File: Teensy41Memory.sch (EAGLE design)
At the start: 17 parts, among them IC1 25AA080SN, IC2 25AA080SN, IC3 25AA080SN, IC4 25AA080SN, IC5 25AA080SN, IC6 25AA080SN, IC7 25AA080SN, IC8 25AA080SN, IC9 74AC138D

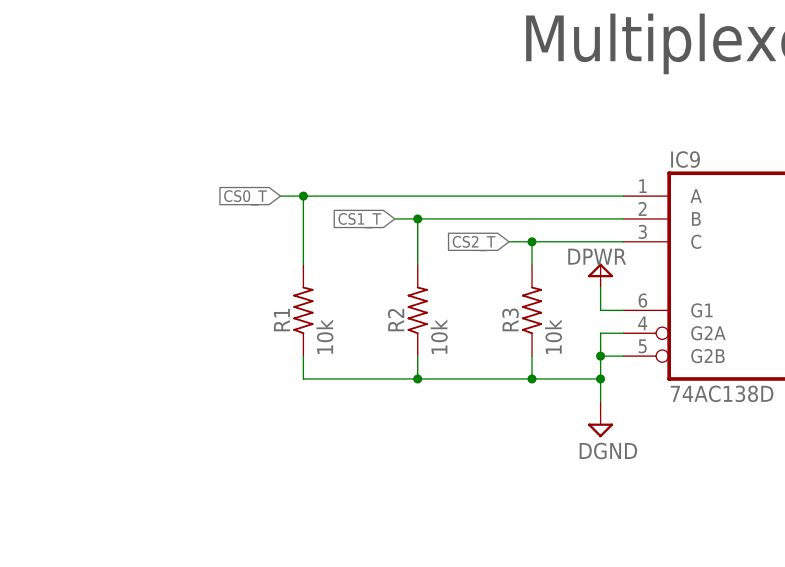
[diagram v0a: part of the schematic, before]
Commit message: Breakout pin 4 of 74AC138 to disable all CS
It is now possible to set all eight chip selects HIGH on the output of 74AC138 by setting pin4 HIGH. The pin is available on Teensy 4.1 pin 5.
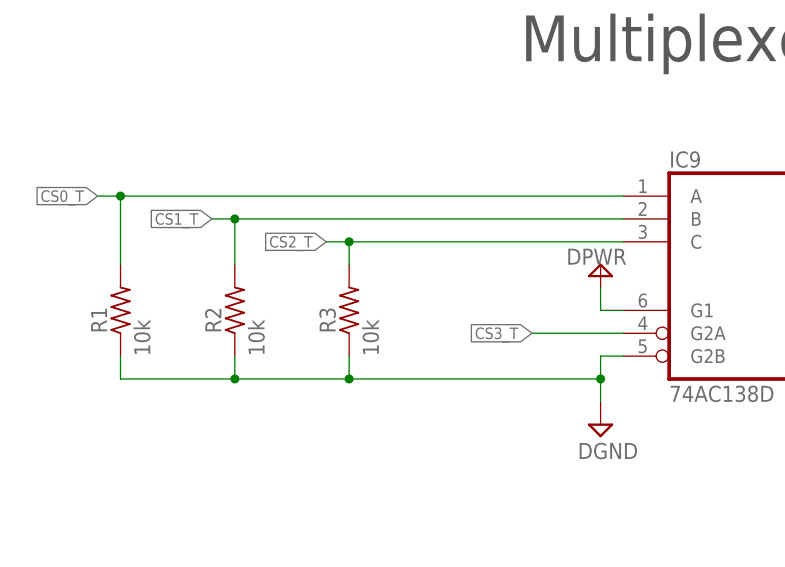
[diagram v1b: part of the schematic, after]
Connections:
- new net CS3_T: IC9A.G2A
- net DGND: no longer IC9A.G2A
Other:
- moved on the sheet: R1, R2, R3
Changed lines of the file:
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@@
 <setting verticaltext="up"/>
 </settings>
-<grid distance="0.1" unitdist="inch" unit="inch" style="lines" multiple="1" display="yes" altdistance="0.01" altunitdist="inch" altunit="inch"/>
+<grid distance="0.1" unitdist="inch" unit="inch" style="lines" multiple="1" display="no" altdistance="0.01" altunitdist="inch" altunit="inch"/>
 <layers>
 <layer number="1" name="Top" color="4" fill="1" visible="no" active="no"/>
@@
 <instance part="FRAME1" gate="G$2" x="325.12" y="0"/>
 <instance part="C1" gate="G$1" x="68.58" y="114.3"/>
-<instance part="R3" gate="G$1" x="66.04" y="180.34" rot="R90"/>
-<instance part="R1" gate="G$1" x="40.64" y="180.34" rot="R90"/>
-<instance part="R2" gate="G$1" x="53.34" y="180.34" rot="R90"/>
+<instance part="R3" gate="G$1" x="45.72" y="180.34" rot="R90"/>
+<instance part="R1" gate="G$1" x="20.32" y="180.34" rot="R90"/>
+<instance part="R2" gate="G$1" x="33.02" y="180.34" rot="R90"/>
 <instance part="C2" gate="G$1" x="78.74" y="114.3"/>
 <instance part="IC1" gate="G$1" x="180.34" y="246.38"/>
@@
 <wire x1="76.2" y1="175.26" x2="73.66" y2="175.26" width="0.1524" layer="91"/>
 <wire x1="73.66" y1="175.26" x2="73.66" y2="172.72" width="0.1524" layer="91"/>
-<pinref part="IC9" gate="A" pin="G2A"/>
 <wire x1="73.66" y1="172.72" x2="73.66" y2="170.18" width="0.1524" layer="91"/>
-<wire x1="76.2" y1="177.8" x2="73.66" y2="177.8" width="0.1524" layer="91"/>
-<wire x1="73.66" y1="177.8" x2="73.66" y2="175.26" width="0.1524" layer="91"/>
-<junction x="73.66" y="175.26"/>
 <pinref part="R1" gate="G$1" pin="1"/>
-<wire x1="40.64" y1="175.26" x2="40.64" y2="172.72" width="0.1524" layer="91"/>
-<wire x1="40.64" y1="172.72" x2="53.34" y2="172.72" width="0.1524" layer="91"/>
+<wire x1="20.32" y1="175.26" x2="20.32" y2="172.72" width="0.1524" layer="91"/>
+<wire x1="20.32" y1="172.72" x2="33.02" y2="172.72" width="0.1524" layer="91"/>
 <junction x="73.66" y="172.72"/>
 <pinref part="R2" gate="G$1" pin="1"/>
-<wire x1="53.34" y1="172.72" x2="66.04" y2="172.72" width="0.1524" layer="91"/>
-<wire x1="66.04" y1="172.72" x2="73.66" y2="172.72" width="0.1524" layer="91"/>
-<wire x1="53.34" y1="175.26" x2="53.34" y2="172.72" width="0.1524" layer="91"/>
-<junction x="53.34" y="172.72"/>
+<wire x1="33.02" y1="172.72" x2="45.72" y2="172.72" width="0.1524" layer="91"/>
+<wire x1="45.72" y1="172.72" x2="73.66" y2="172.72" width="0.1524" layer="91"/>
+<wire x1="33.02" y1="175.26" x2="33.02" y2="172.72" width="0.1524" layer="91"/>
+<junction x="33.02" y="172.72"/>
 <pinref part="R3" gate="G$1" pin="1"/>
-<wire x1="66.04" y1="175.26" x2="66.04" y2="172.72" width="0.1524" layer="91"/>
-<junction x="66.04" y="172.72"/>
+<wire x1="45.72" y1="175.26" x2="45.72" y2="172.72" width="0.1524" layer="91"/>
+<junction x="45.72" y="172.72"/>
 </segment>
 </net>
@@
 <segment>
 <pinref part="IC9" gate="A" pin="A"/>
-<wire x1="76.2" y1="193.04" x2="40.64" y2="193.04" width="0.1524" layer="91"/>
-<label x="38.1" y="193.04" size="1.27" layer="95" ratio="12" rot="R180" xref="yes"/>
+<wire x1="76.2" y1="193.04" x2="20.32" y2="193.04" width="0.1524" layer="91"/>
+<label x="17.78" y="193.04" size="1.27" layer="95" ratio="12" rot="R180" xref="yes"/>
 <pinref part="R1" gate="G$1" pin="2"/>
-<wire x1="40.64" y1="193.04" x2="38.1" y2="193.04" width="0.1524" layer="91"/>
-<wire x1="40.64" y1="185.42" x2="40.64" y2="193.04" width="0.1524" layer="91"/>
-<junction x="40.64" y="193.04"/>
+<wire x1="20.32" y1="193.04" x2="17.78" y2="193.04" width="0.1524" layer="91"/>
+<wire x1="20.32" y1="185.42" x2="20.32" y2="193.04" width="0.1524" layer="91"/>
+<junction x="20.32" y="193.04"/>
 </segment>
 </net>
@@
 <segment>
 <pinref part="IC9" gate="A" pin="B"/>
-<wire x1="76.2" y1="190.5" x2="53.34" y2="190.5" width="0.1524" layer="91"/>
-<label x="50.8" y="190.5" size="1.27" layer="95" ratio="12" rot="R180" xref="yes"/>
+<wire x1="76.2" y1="190.5" x2="33.02" y2="190.5" width="0.1524" layer="91"/>
+<label x="30.48" y="190.5" size="1.27" layer="95" ratio="12" rot="R180" xref="yes"/>
 <pinref part="R2" gate="G$1" pin="2"/>
-<wire x1="53.34" y1="190.5" x2="50.8" y2="190.5" width="0.1524" layer="91"/>
-<wire x1="53.34" y1="185.42" x2="53.34" y2="190.5" width="0.1524" layer="91"/>
-<junction x="53.34" y="190.5"/>
+<wire x1="33.02" y1="190.5" x2="30.48" y2="190.5" width="0.1524" layer="91"/>
+<wire x1="33.02" y1="185.42" x2="33.02" y2="190.5" width="0.1524" layer="91"/>
+<junction x="33.02" y="190.5"/>
 </segment>
 </net>
@@
 <segment>
 <pinref part="IC9" gate="A" pin="C"/>
-<wire x1="76.2" y1="187.96" x2="66.04" y2="187.96" width="0.1524" layer="91"/>
-<label x="63.5" y="187.96" size="1.27" layer="95" ratio="12" rot="R180" xref="yes"/>
+<wire x1="76.2" y1="187.96" x2="45.72" y2="187.96" width="0.1524" layer="91"/>
+<label x="43.18" y="187.96" size="1.27" layer="95" ratio="12" rot="R180" xref="yes"/>
 <pinref part="R3" gate="G$1" pin="2"/>
-<wire x1="66.04" y1="187.96" x2="63.5" y2="187.96" width="0.1524" layer="91"/>
-<wire x1="66.04" y1="185.42" x2="66.04" y2="187.96" width="0.1524" layer="91"/>
-<junction x="66.04" y="187.96"/>
-</segment>
-</net>
+<wire x1="45.72" y1="187.96" x2="43.18" y2="187.96" width="0.1524" layer="91"/>
+<wire x1="45.72" y1="185.42" x2="45.72" y2="187.96" width="0.1524" layer="91"/>
+<junction x="45.72" y="187.96"/>
+</segment>
+</net>
+<net name="CS3_T" class="0">
+<segment>
+<pinref part="IC9" gate="A" pin="G2A"/>
+<wire x1="76.2" y1="177.8" x2="66.04" y2="177.8" width="0.1524" layer="91"/>
+<label x="66.04" y="177.8" size="1.27" layer="95" font="vector" ratio="12" rot="R180" xref="yes"/>
+</segment>
+</net>
